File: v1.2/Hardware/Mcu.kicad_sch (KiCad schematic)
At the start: 15 parts, among them J2 L-KLS1-207-2-08-S, J5 Conn_01x04, U17 STM32F334C8Tx, Y1 8MHz

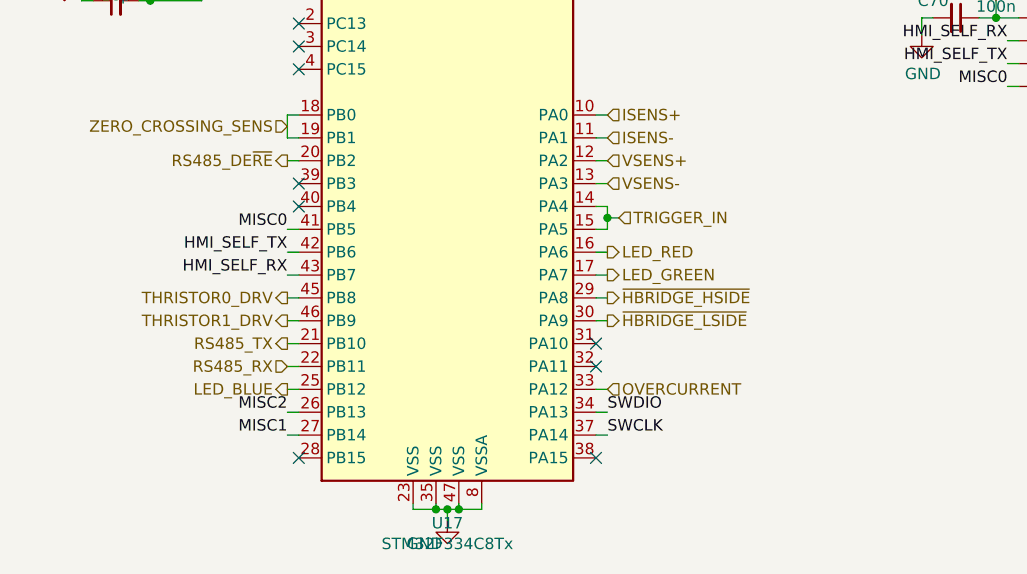
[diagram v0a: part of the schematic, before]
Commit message: Addition of firmware to v1.2(not tested)
+Addition of power tracking(with duty cycle control).
+Addition of resonance freq tracking(via proprietary algorithm relied on active and reactive power measurements)
+Quality factor monitoring
+Power boost when loaded(idle and loaded modes)
+Much better frequency resolution(less than 1Hz)
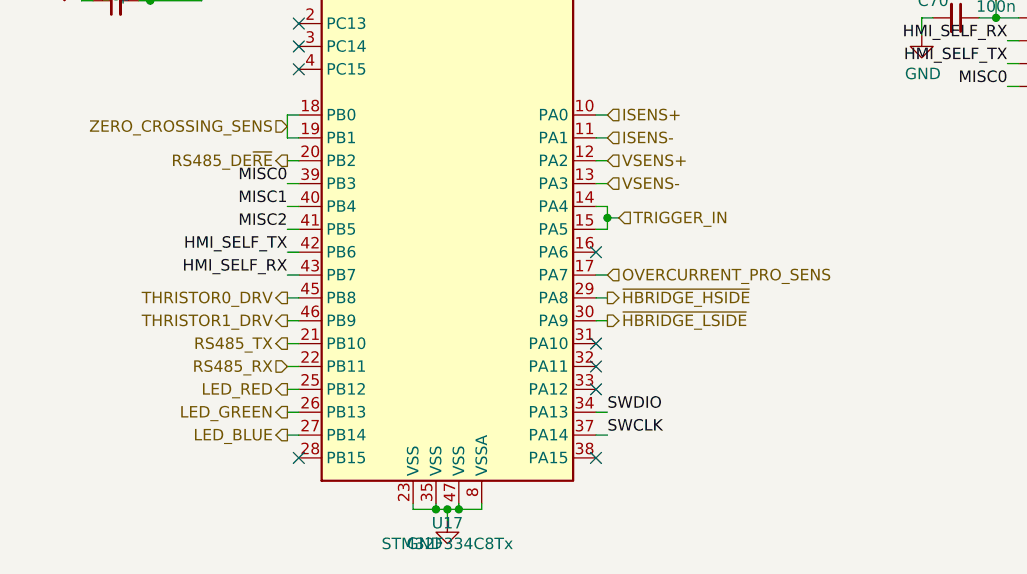
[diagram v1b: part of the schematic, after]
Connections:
- net LED_BLUE: now also U17.27 (PB14); no longer U17.25 (PB12)
- net LED_GREEN: now also U17.26 (PB13); no longer U17.17 (PA7)
- net LED_RED: now also U17.25 (PB12); no longer U17.16 (PA6)
- net MISC0: now also U17.39 (PB3); no longer U17.41 (PB5)
- net MISC1: now also U17.40 (PB4); no longer U17.27 (PB14)
- net MISC2: now also U17.41 (PB5); no longer U17.26 (PB13)
- net OVERCURRENT: no longer names the net of U17.33 (PA12)
- new net OVERCURRENT_PRO_SENS: U17.17 (PA7)

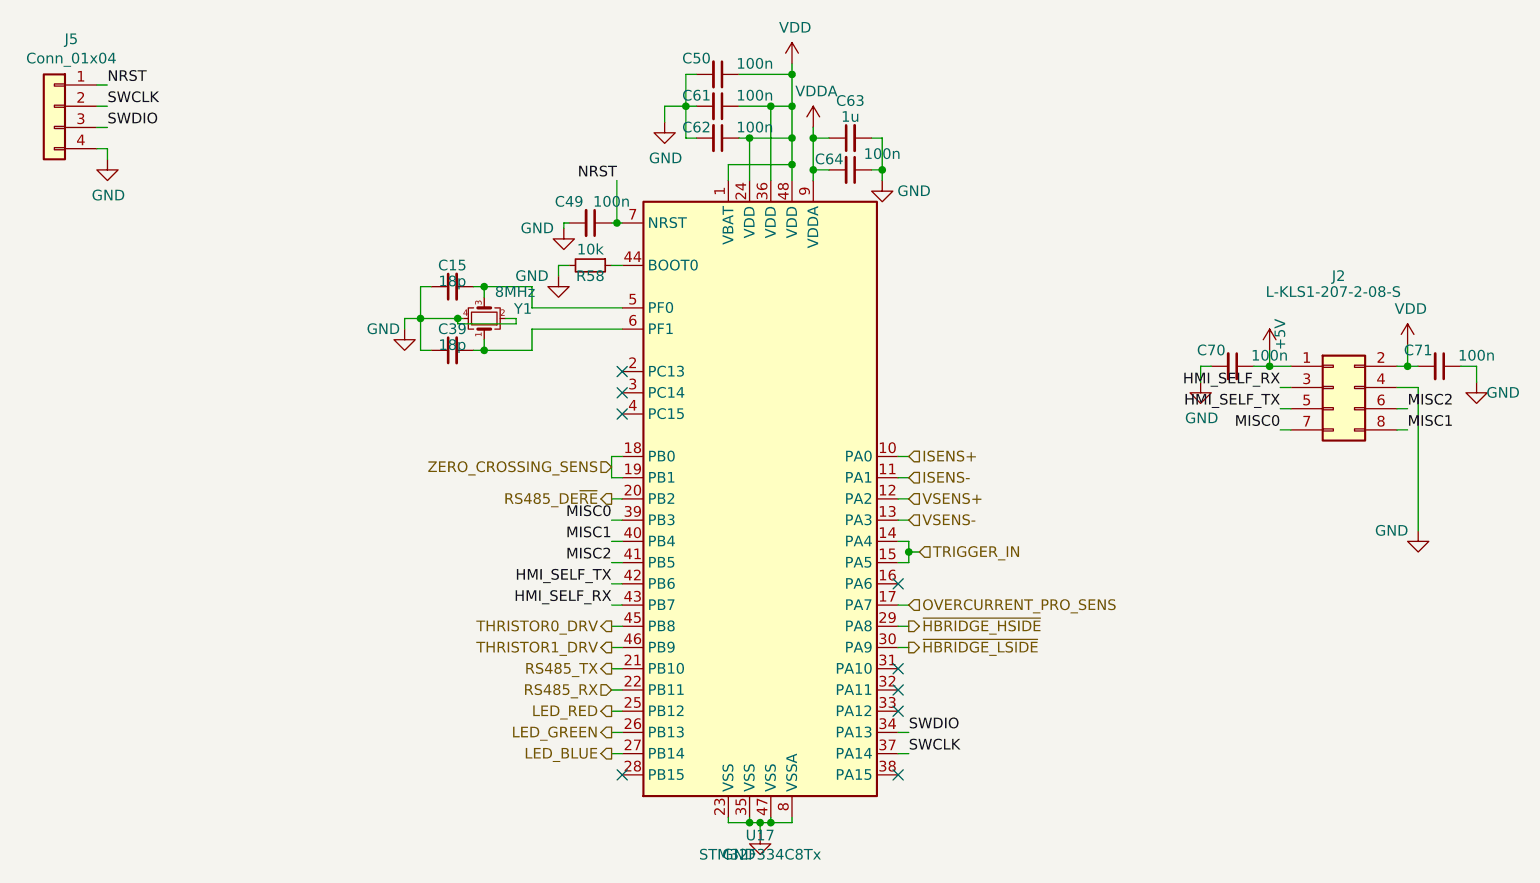
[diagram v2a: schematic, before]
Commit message: Redesign.
+Cli interface.
+Modularity improvement(complex number and pid modules created)
+Range change.
+Core-Lattice seperated. 
+Improvement of the control function
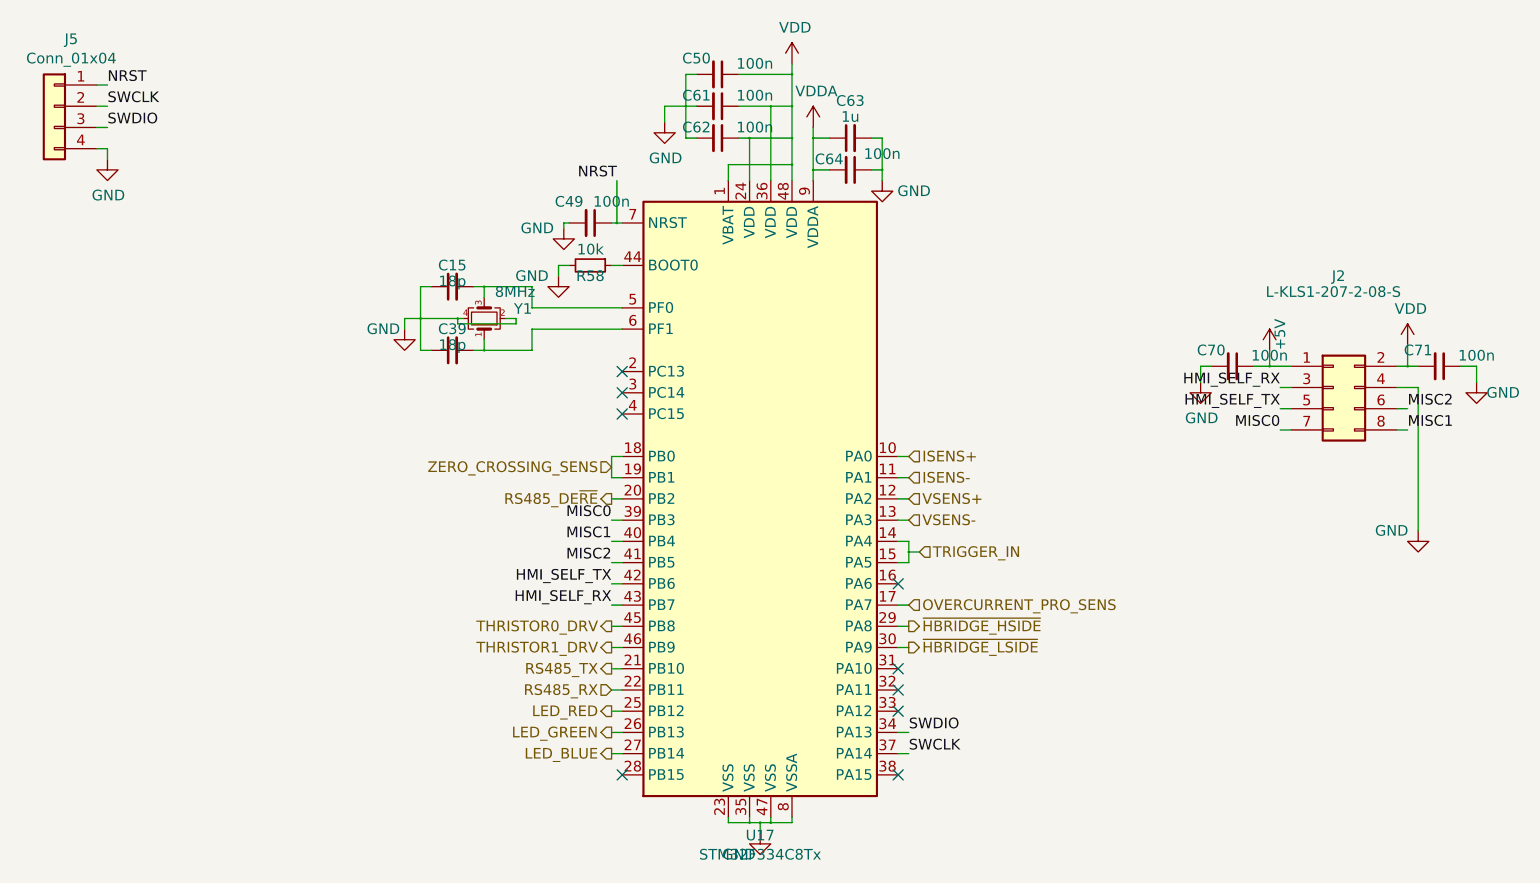
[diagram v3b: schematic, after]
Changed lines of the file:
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@@
-(kicad_sch (version 20200618) (host eeschema "5.99.0-unknown-f3f1740~101~ubuntu18.04.1")
+(kicad_sch (version 20200828) (generator eeschema)
   (page 5 8)
   (paper "A4")
-  (junction (at 109.855 66.04) (diameter 0) (color 0 0 0 0))
-  (junction (at 114.3 66.04) (diameter 0) (color 0 0 0 0))
-  (junction (at 117.475 62.23) (diameter 0) (color 0 0 0 0))
-  (junction (at 117.475 69.85) (diameter 0) (color 0 0 0 0))
-  (junction (at 133.35 54.61) (diameter 0) (color 0 0 0 0))
-  (junction (at 141.605 40.64) (diameter 0) (color 0 0 0 0))
-  (junction (at 149.225 44.45) (diameter 0) (color 0 0 0 0))
-  (junction (at 149.225 126.365) (diameter 0) (color 0 0 0 0))
-  (junction (at 150.495 126.365) (diameter 0) (color 0 0 0 0))
-  (junction (at 151.765 40.64) (diameter 0) (color 0 0 0 0))
-  (junction (at 151.765 126.365) (diameter 0) (color 0 0 0 0))
-  (junction (at 154.305 36.83) (diameter 0) (color 0 0 0 0))
-  (junction (at 154.305 40.64) (diameter 0) (color 0 0 0 0))
-  (junction (at 154.305 44.45) (diameter 0) (color 0 0 0 0))
-  (junction (at 154.305 47.625) (diameter 0) (color 0 0 0 0))
-  (junction (at 156.845 44.45) (diameter 0) (color 0 0 0 0))
-  (junction (at 156.845 48.26) (diameter 0) (color 0 0 0 0))
-  (junction (at 165.1 48.26) (diameter 0) (color 0 0 0 0))
-  (junction (at 168.275 93.98) (diameter 0) (color 0 0 0 0))
-  (junction (at 211.455 71.755) (diameter 0) (color 0 0 0 0))
-  (junction (at 227.965 71.755) (diameter 0) (color 0 0 0 0))
-  (no_connect (at 167.005 113.03))
+  (junction (at 109.855 66.04) (diameter 0.3048) (color 0 0 0 0))
+  (junction (at 114.3 66.04) (diameter 0.3048) (color 0 0 0 0))
+  (junction (at 117.475 62.23) (diameter 0.3048) (color 0 0 0 0))
+  (junction (at 117.475 69.85) (diameter 0.3048) (color 0 0 0 0))
+  (junction (at 133.35 54.61) (diameter 0.3048) (color 0 0 0 0))
+  (junction (at 141.605 40.64) (diameter 0.3048) (color 0 0 0 0))
+  (junction (at 149.225 44.45) (diameter 0.3048) (color 0 0 0 0))
+  (junction (at 149.225 126.365) (diameter 0.3048) (color 0 0 0 0))
+  (junction (at 150.495 126.365) (diameter 0.3048) (color 0 0 0 0))
+  (junction (at 151.765 40.64) (diameter 0.3048) (color 0 0 0 0))
+  (junction (at 151.765 126.365) (diameter 0.3048) (color 0 0 0 0))
+  (junction (at 154.305 36.83) (diameter 0.3048) (color 0 0 0 0))
+  (junction (at 154.305 40.64) (diameter 0.3048) (color 0 0 0 0))
+  (junction (at 154.305 44.45) (diameter 0.3048) (color 0 0 0 0))
+  (junction (at 154.305 47.625) (diameter 0.3048) (color 0 0 0 0))
+  (junction (at 156.845 44.45) (diameter 0.3048) (color 0 0 0 0))
+  (junction (at 156.845 48.26) (diameter 0.3048) (color 0 0 0 0))
+  (junction (at 165.1 48.26) (diameter 0.3048) (color 0 0 0 0))
+  (junction (at 168.275 93.98) (diameter 0.3048) (color 0 0 0 0))
+  (junction (at 211.455 71.755) (diameter 0.3048) (color 0 0 0 0))
+  (junction (at 227.965 71.755) (diameter 0.3048) (color 0 0 0 0))
   (no_connect (at 133.985 74.93))
-  (no_connect (at 133.985 120.65))
+  (no_connect (at 167.005 107.95))
   (no_connect (at 167.005 120.65))
   (no_connect (at 167.005 97.79))
+  (no_connect (at 133.985 77.47))
+  (no_connect (at 133.985 120.65))
+  (no_connect (at 133.985 72.39))
   (no_connect (at 167.005 110.49))
-  (no_connect (at 133.985 77.47))
-  (no_connect (at 133.985 72.39))
-  (no_connect (at 167.005 107.95))
+  (no_connect (at 167.005 113.03))
   (wire (pts (xy 71.12 38.1) (xy 72.39 38.1))
     (stroke (width 0) (type solid) (color 0 0 0 0))
